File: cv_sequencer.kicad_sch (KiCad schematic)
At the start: 48 parts, among them J10 3096_USBC_RA_SMD, J11 4005_SWD_Header, J9 3086_Connector_Eurorack_Power, U1 3097_TFT_Display_SPI, U2 3093_MIC5225_3v3, U3 4002_RP2040, Y1 4004-Crystal-12MHz_GND24

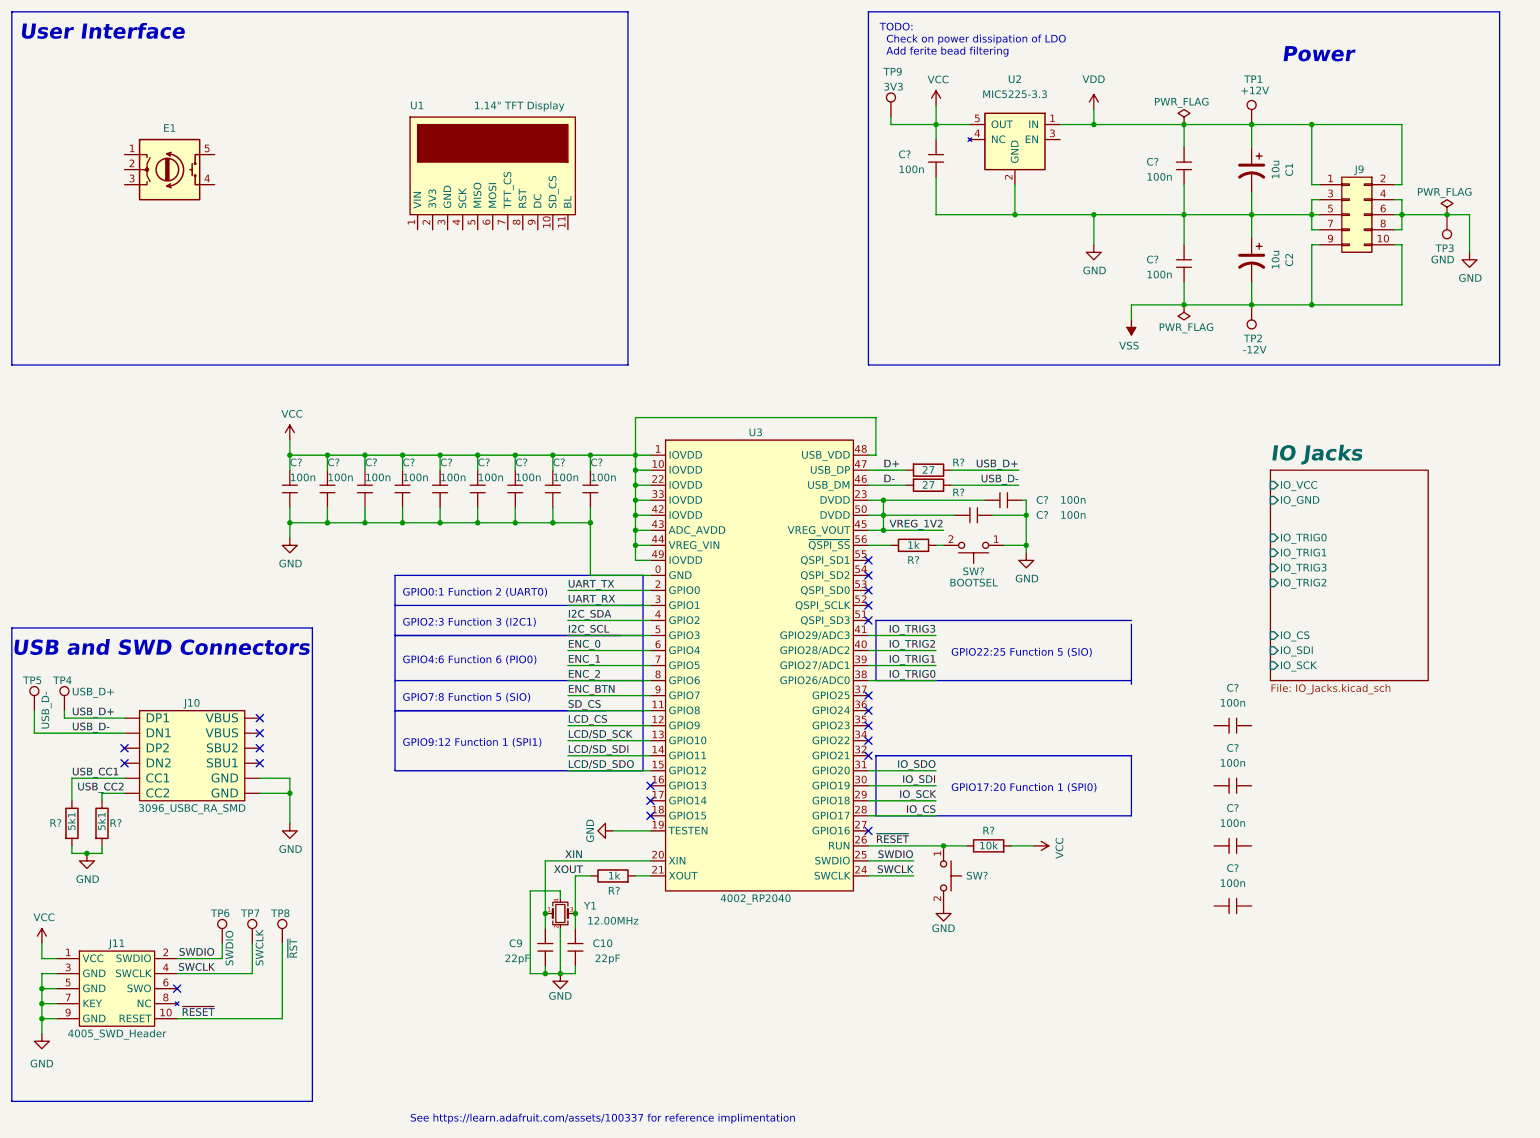
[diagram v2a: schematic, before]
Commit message: finished schematic (still needs double checking)
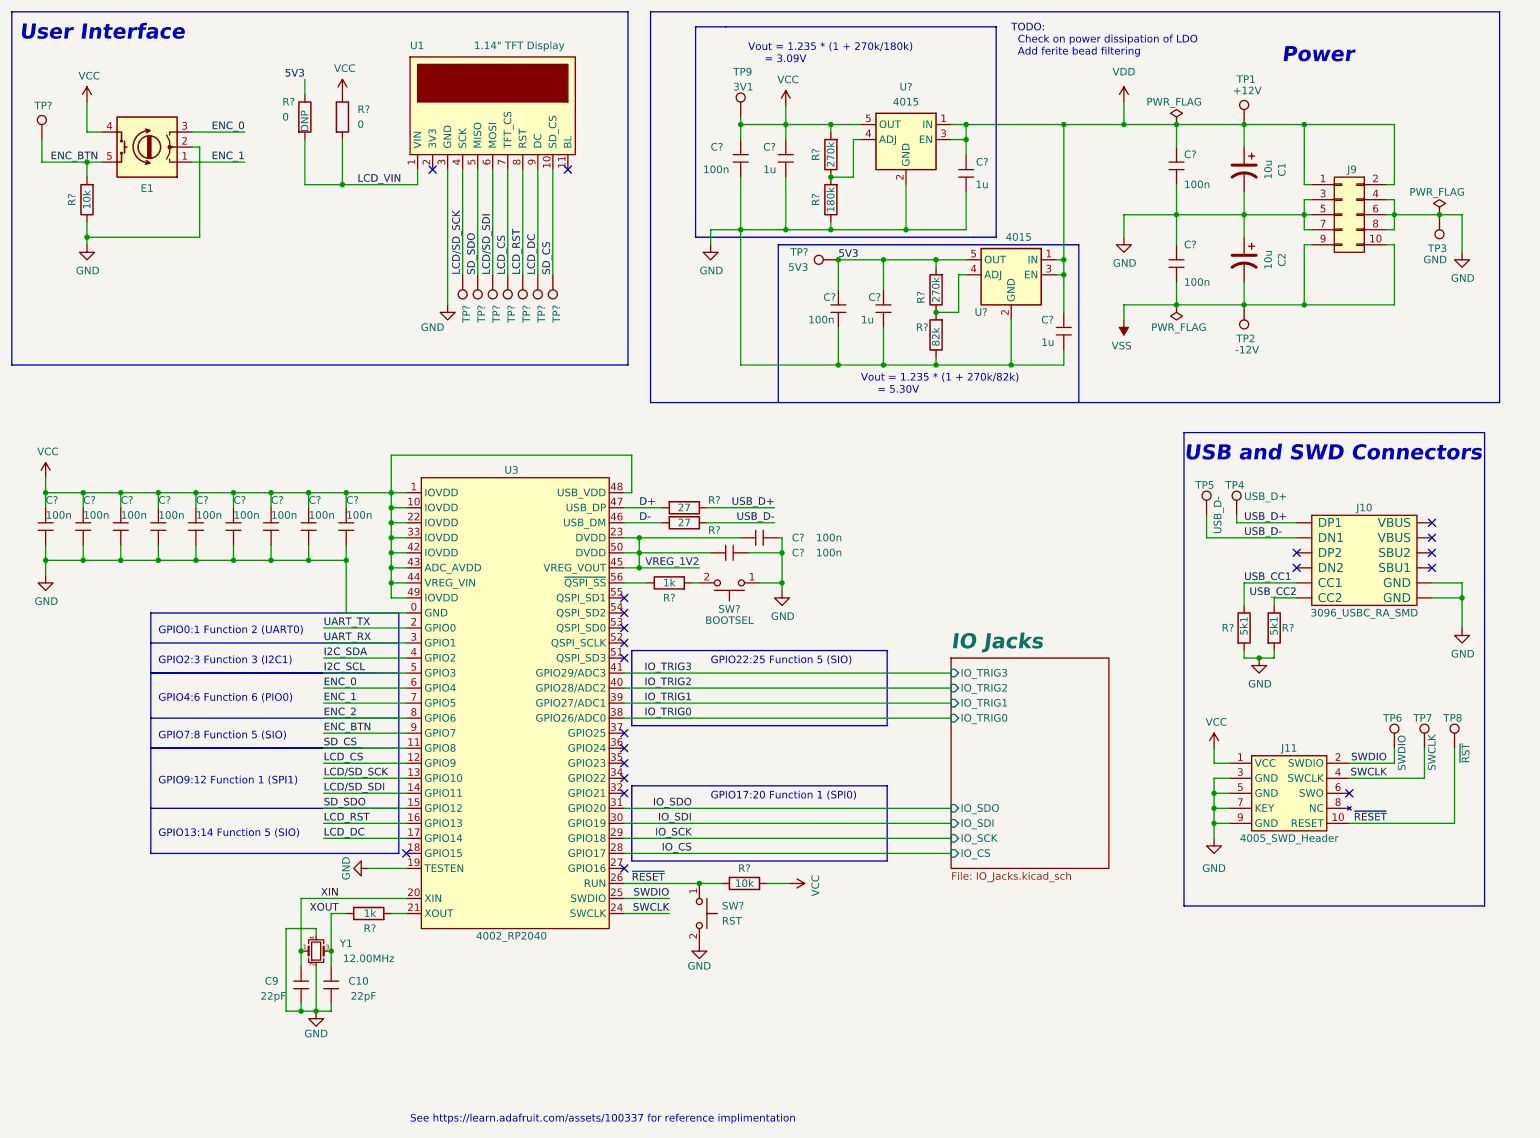
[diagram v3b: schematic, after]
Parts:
- removed C? (x4): 3089_Capacitor_100n_16V_0402, Shulltronics_Generics:C_0402_HandSolder, symbol Shulltronics_Passives:3089_Capacitor_100n_16V_0402
- removed U2: 3093_MIC5225_3v3, Shulltronics_Regulators:3093_MIC5225_3v3_LDO, symbol Shulltronics_Regulators:3093_MIC5225_3v3
- added C? (x4): 4013_Capacitor_1u_16V_0402, Shulltronics_Generics:C_0402_HandSolder, symbol Shulltronics_Passives:4013_Capacitor_1u_16V_0402
- added C?: 3089_Capacitor_100n_16V_0402, Shulltronics_Generics:C_0402_HandSolder, symbol Shulltronics_Passives:3089_Capacitor_100n_16V_0402
- added R?: 4021_Resistor_SMD_Jumper, Shulltronics_Passives:Resistor_0402, symbol Shulltronics_Passives:4021_Resistor_SMD_Jumper
- added R?: DNP, Shulltronics_Passives:Resistor_0402, symbol Shulltronics_Passives:4021_Resistor_SMD_Jumper
- added R? (x2): 4019_Resistor_SMD_270k_0.125W_1%, Shulltronics_Passives:Resistor_0402, symbol Shulltronics_Passives:4019_Resistor_SMD_270k_0.125W_1%
- added R?: 4020_Resistor_SMD_180k_0.125W_1%, Shulltronics_Passives:Resistor_0402, symbol Shulltronics_Passives:4020_Resistor_SMD_180k_0.125W_1%
- added R?: 4008_Resistor_SMD_10k_0.125W_1%, Shulltronics_Passives:Resistor_0402, symbol Shulltronics_Passives:4008_Resistor_SMD_10k_0.125W_1%
- added R?: 4018_Resistor_SMD_82k_0.125W_1%, Shulltronics_Passives:Resistor_0402, symbol Shulltronics_Passives:4018_Resistor_SMD_82k_0.125W_1%
- added TP?: SD_SDO, Shulltronics_Generics:TestPoint_Pad_D2.0mm, symbol Shulltronics_Sch_Symbols:TestPoint
- added TP?: ENC_BTN, Shulltronics_Generics:TestPoint_Pad_D2.0mm, symbol Shulltronics_Sch_Symbols:TestPoint
- added TP?: SD_CS, Shulltronics_Generics:TestPoint_Pad_D2.0mm, symbol Shulltronics_Sch_Symbols:TestPoint
- added TP?: LCD_DC, Shulltronics_Generics:TestPoint_Pad_D2.0mm, symbol Shulltronics_Sch_Symbols:TestPoint
- added TP?: LCD/SD_SDI, Shulltronics_Generics:TestPoint_Pad_D2.0mm, symbol Shulltronics_Sch_Symbols:TestPoint
- added TP?: LCD_RST, Shulltronics_Generics:TestPoint_Pad_D2.0mm, symbol Shulltronics_Sch_Symbols:TestPoint
- added TP?: LCD/SD_SCK, Shulltronics_Generics:TestPoint_Pad_D2.0mm, symbol Shulltronics_Sch_Symbols:TestPoint
- added TP?: LCD_CS, Shulltronics_Generics:TestPoint_Pad_D2.0mm, symbol Shulltronics_Sch_Symbols:TestPoint
- added TP?: 5V3, Shulltronics_Generics:TestPoint_Pad_D2.0mm, symbol Shulltronics_Sch_Symbols:TestPoint
- added U? (x2): 4015_Adjustable_Reg_500mA_SOT-23-5, Shulltronics_Generics:SOT-23-5, symbol Shulltronics_Regulators:4015_Adjustable_Reg_500mA_SOT-23-5
- SW?: value 4012_PushButton_NO_SMD -> RST
- TP9: value 3V3 -> 3V1
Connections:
- net LCD/SD_SDO is gone; now on net SD_SDO: U3.15 (GPIO12)
- net ENC_0: now also E1.3
- net ENC_1: now also E1.1
- net ENC_BTN: now also E1.5, R?.2, TP?.1
- net GND: now also E1.2, U1.3 (GND), C?.1, C?.1, C?.1, C?.1, C?.1, R?.1, R?.1, R?.1, U?.2 (GND), U?.2 (GND)
- net LCD_CS: now also U1.7 (TFT_CS), TP?.1
- net LCD/SD_SCK: now also U1.4 (SCK), TP?.1
- net LCD/SD_SDI: now also U1.6 (MOSI), TP?.1
- net SD_CS: now also U1.10 (SD_CS), TP?.1
- net VCC: now also E1.4, C?.2, R?.1, R?.2, U?.5 (OUT)
- net VDD: now also C?.2, C?.2, U?.1 (IN), U?.1 (IN), U?.3 (EN), U?.3 (EN)
- net LCD_VIN: now reaches U1.1 (VIN)
- net LCD_VIN: now also R?.2, R?.2
- net SD_SDO: now reaches U1.5 (MISO)
- net SD_SDO: now also TP?.1
- net LCD_RST: now reaches U1.8 (RST)
- net LCD_RST: now also U3.16 (GPIO13), TP?.1
- net LCD_DC: now reaches U1.9 (DC)
- net LCD_DC: now also U3.17 (GPIO14), TP?.1
- new net: R?.1, R?.2, U?.4 (ADJ) (x2)
- new net 5V3: C?.2, C?.2, R?.1, R?.2, TP?.1, U?.5 (OUT)
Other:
- sheet IO Jacks ports: added IO_SDO; removed IO_GND, IO_VCC
- note added: "GPIO13:14 Function 5 (SIO)"
- note added: "Vout = 1.235 * (1 + 270k/180k) = 3.09V"
- note added: "Vout = 1.235 * (1 + 270k/82k) = 5.30V"
- moved on the sheet: C1, C10, C2, C9, C?, E1, J10, J11, J9, R?, SW?, TP1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

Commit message: ran ERC, minimal errors. Imported footprints and started grouping them
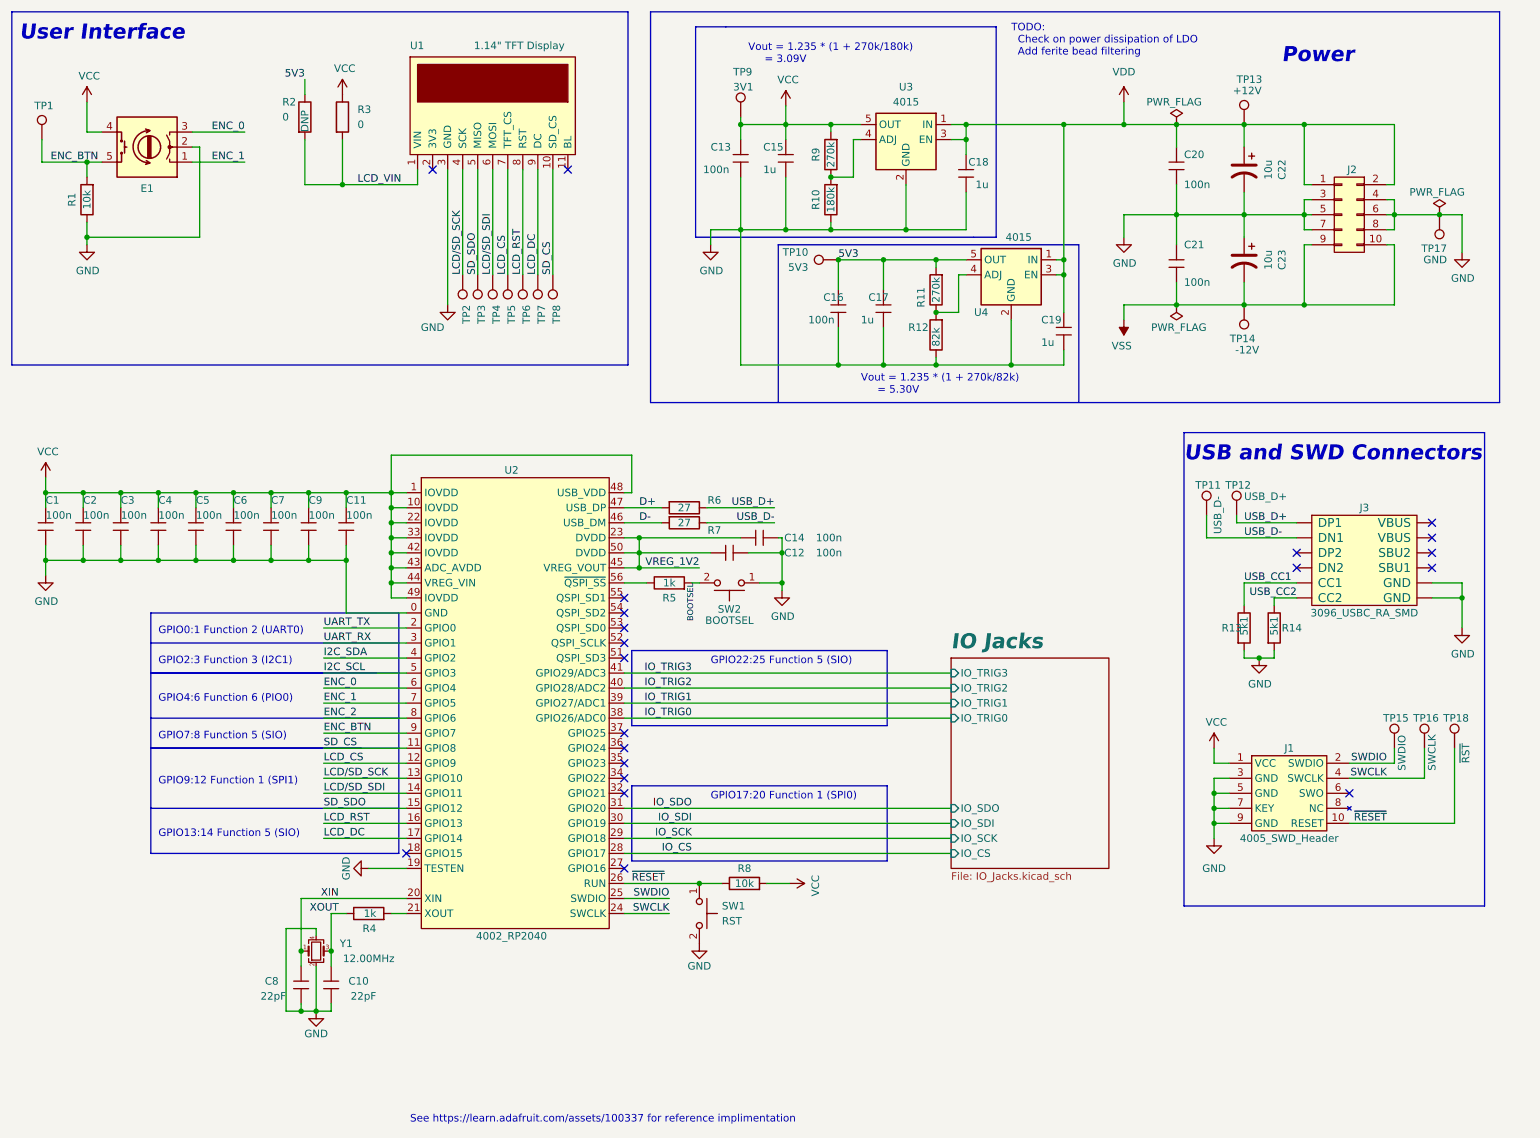
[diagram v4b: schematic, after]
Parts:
- R1, R10, R11, R12, R13, R14, R2, R3, R4, R5, R6, R7, R8, R9: renamed from R?; footprint Shulltronics_Passives:Resistor_0402 -> Shulltronics_Generics:RES-0402
- gave numbers to parts that had none: 32
- renumbered C1 to C22, C2 to C23, C9 to C8, J11 to J1, J9 to J2, J10 to J3, TP5 to TP11, TP4 to TP12, TP1 to TP13, TP2 to TP14, TP6 to TP15, TP7 to TP16, TP3 to TP17, TP8 to TP18, U3 to U2
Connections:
- net BOOTSEL: now reaches R5.2, SW2.2

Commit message: more work on pcb, added some TODO notes to schematic
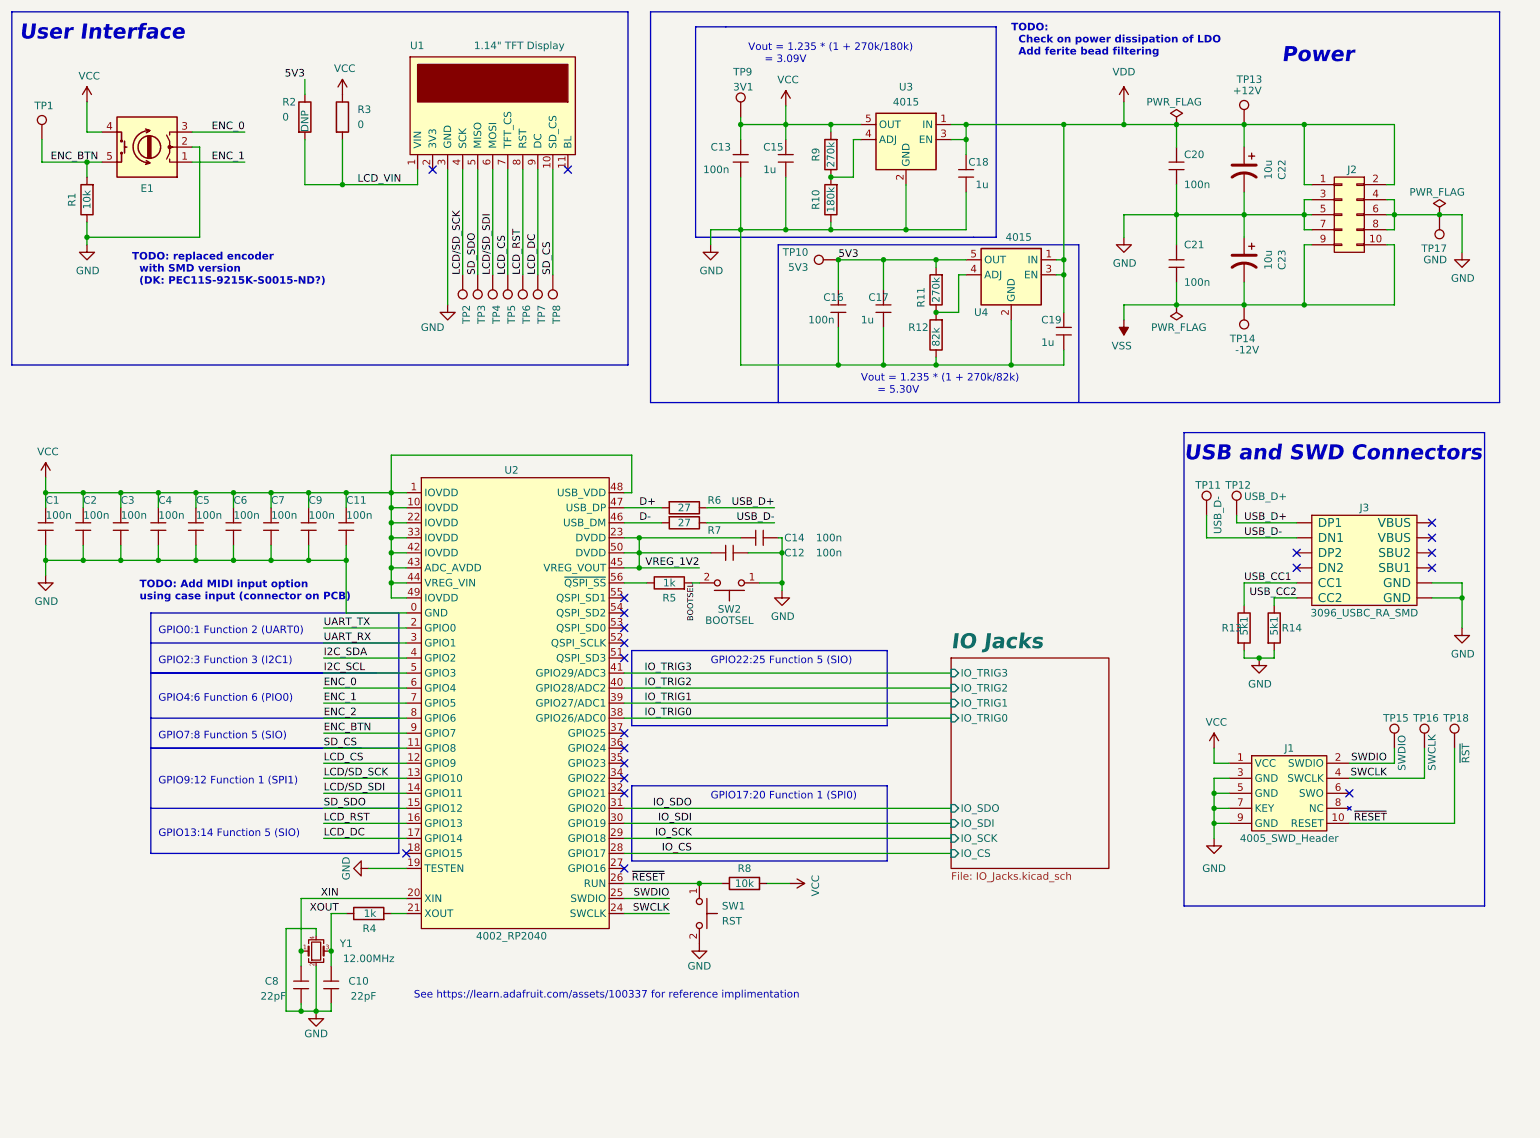
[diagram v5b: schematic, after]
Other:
- note added: "TODO: Add MIDI input option using case input (connector on PCB)"
- note added: "TODO: replaced encoder with SMD version (DK: PEC11S-9215K-S0015-ND?)"
- company: (none) -> Shulltronics
- title: (none) -> Binary CV Sequencer
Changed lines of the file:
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@@
 (kicad_sch (version 20211123) (generator eeschema)
   (paper "USLetter")
+  (title_block
+    (title "Binary CV Sequencer")
+    (date "2022-03-11")
+    (rev "0.1")
+    (company "Shulltronics")
+  )
   (junction (at 182.88 73.66) (diameter 0) (color 0 0 0 0)
   )
@@
   )
   (text "See https://learn.adafruit.com/assets/100337 for reference implimentation"
-    (at 81.28 201.93 0)
+    (at 81.915 180.975 0)
     (effects (font (size 1.27 1.27)) (justify left bottom))
   )
@@
     (effects (font (size 1.27 1.27)) (justify left bottom))
   )
+  (text "TODO: replaced encoder\n  with SMD version\n  (DK: PEC11S-9215K-S0015-ND?)"
+    (at 34.29 60.325 0)
+    (effects (font (size 1.27 1.27) (thickness 0.254) bold) (justify left bottom))
+  )
   (text "USB and SWD Connectors" (at 212.09 90.17 0)
     (effects (font (size 2.54 2.54) (thickness 0.508) bold italic) (justify left bottom))
@@
     (effects (font (size 1.27 1.27)) (justify left bottom))
   )
+  (text "TODO: Add MIDI input option\nusing case input (connector on PCB)"
+    (at 35.56 113.665 0)
+    (effects (font (size 1.27 1.27) (thickness 0.254) bold) (justify left bottom))
+  )
   (text "GPIO0:1 Function 2 (UART0)" (at 38.735 119.38 0)
     (effects (font (size 1.27 1.27)) (justify left bottom))
@@
   (text "TODO:\n  Check on power dissipation of LDO\n  Add ferite bead filtering"
     (at 182.88 21.59 0)
-    (effects (font (size 1.27 1.27)) (justify left bottom))
+    (effects (font (size 1.27 1.27) (thickness 0.254) bold) (justify left bottom))
   )
   (text "GPIO13:14 Function 5 (SIO)" (at 38.735 153.67 0)
